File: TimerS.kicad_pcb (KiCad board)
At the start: 2 copper layers, 140 x 65 mm, 65 parts, among them J1 Power, SW1 Start/Stop, SW2 Reset, U1 74LS90, U11 74LS90, U12 74LS47, U14 NA555P, U15 NA555P, U2 74LS47, U4 L7805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

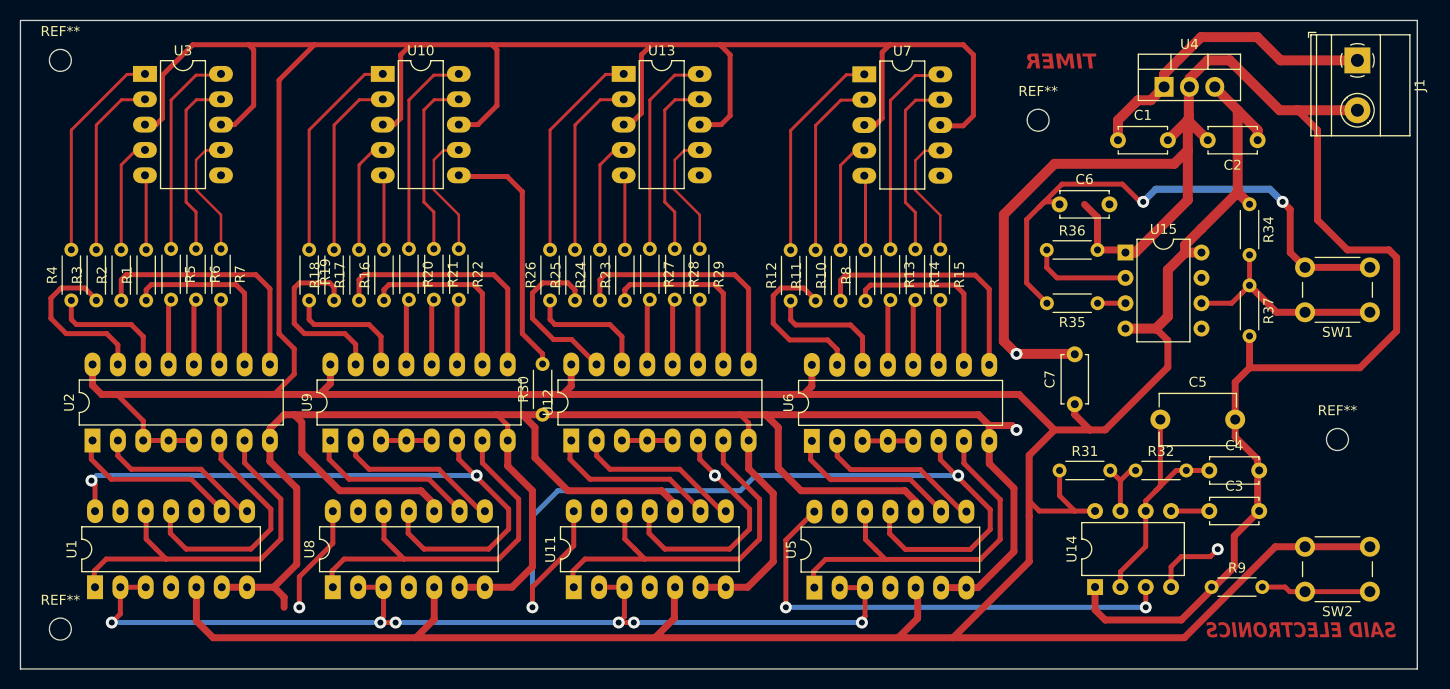
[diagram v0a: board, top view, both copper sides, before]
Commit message: Layout correction
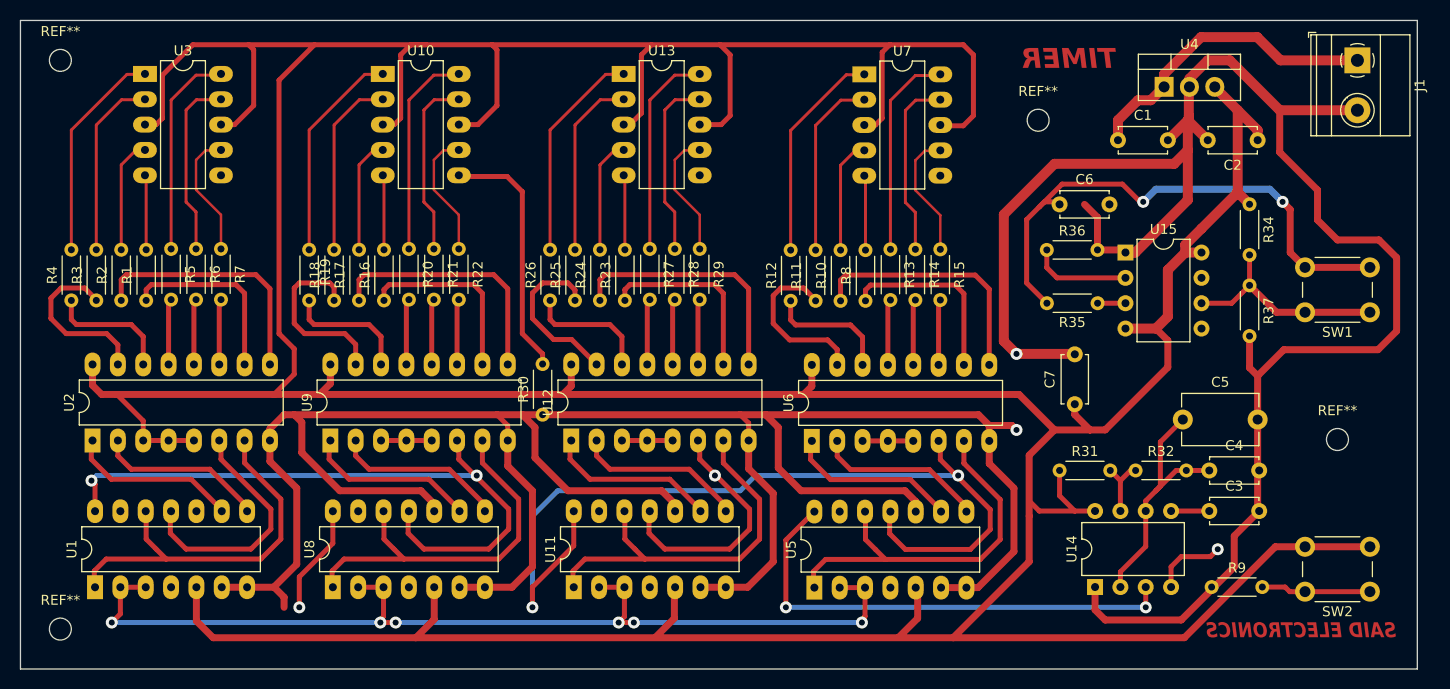
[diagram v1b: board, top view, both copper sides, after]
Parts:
- moved C5 2.25 mm to (180.5, 110.0)
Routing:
- net Net-(U14-THR): track 24.9 -> 25.8 mm
- net GND: track 426.3 -> 425.4 mm
- net Net-(U8-Q2): track 17.3 -> 17.9 mm
- net Net-(U11-Q2): track 17.3 -> 17.9 mm
- net Net-(U5-Q2): track 17.3 -> 17.9 mm
- net Net-(U1-Q2): track 17.3 -> 17.8 mm

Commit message: PDF added
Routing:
- net GND: track 425.4 -> 422.9 mm
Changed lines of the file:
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@@
   (segment (start 139.446 117.39) (end 136.985 114.929) (width 0.7) (layer "F.Cu") (net 19))
   (segment (start 188 110) (end 188 119.014) (width 0.7) (layer "F.Cu") (net 19))
-  (segment (start 89.425 126.805) (end 90.424 127.804) (width 0.7) (layer "F.Cu") (net 19))
   (segment (start 108.01 126.805) (end 110.55 126.805) (width 0.7) (layer "F.Cu") (net 19))
   (segment (start 159.963 126.845) (end 163.576 123.232) (width 0.7) (layer "F.Cu") (net 19))
@@
   (segment (start 138.684 109.516) (end 136.144 109.516) (width 0.7) (layer "F.Cu") (net 19))
   (segment (start 160.02 109.516) (end 138.684 109.516) (width 0.7) (layer "F.Cu") (net 19))
-  (segment (start 90.424 127.804) (end 90.424 128.82) (width 0.7) (layer "F.Cu") (net 19))
   (segment (start 110.55 126.805) (end 113.267 126.805) (width 0.7) (layer "F.Cu") (net 19))
   (segment (start 161.1 110.596) (end 163.386 110.596) (width 0.7) (layer "F.Cu") (net 19))
